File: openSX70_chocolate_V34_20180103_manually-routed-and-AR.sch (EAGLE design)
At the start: 37 parts, among them Q1 5.8A/30V/35mΩ, Q2 5.8A/30V/35mΩ, U1 ATMEGA328P_TQFP, U3 BH1750FVI-TR, Y1 CSTCE16M0V53-R0

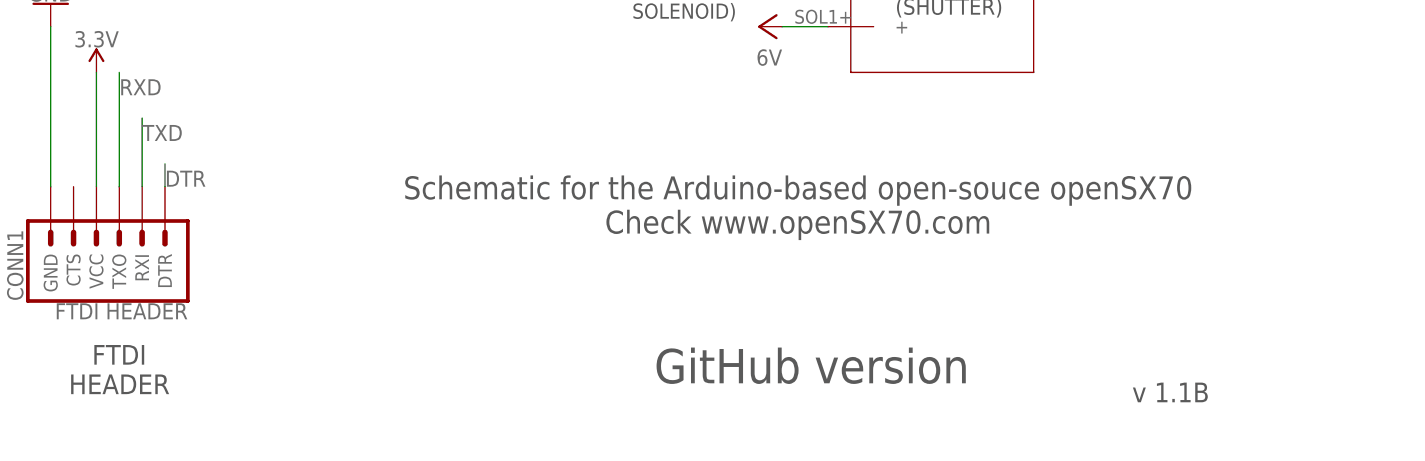
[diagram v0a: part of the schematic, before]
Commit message: Create new 3.4 "chocolate" version. Looks ok, will do more tests and send it for fabrication. Also created gerbers, remember minimun .8mm, better .6mm or .4mm.
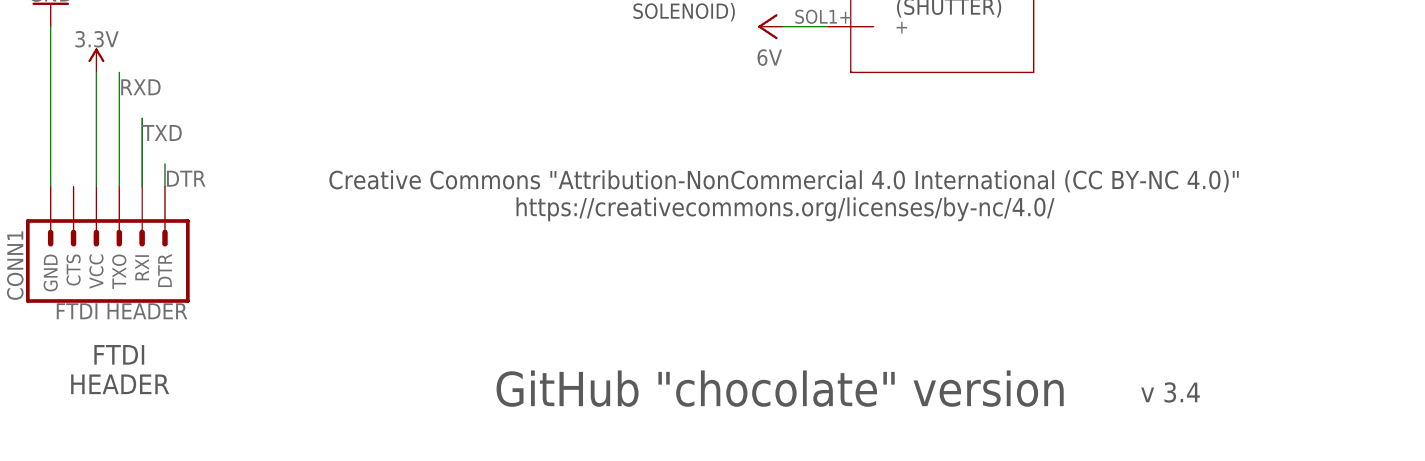
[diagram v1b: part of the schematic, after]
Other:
- note added: "Creative Commons "Attribution-NonCommercial 4.0 International (CC BY-NC 4.0)" https://creativecommons.org/licenses/by-nc/4.0/"
- note added: "GitHub "chocolate" version"
- note added: "v 3.4"
- note removed: "GitHub version"
- note removed: "Schematic for the Arduino-based open-souce openSX70 Check www.openSX70.com"
- note removed: "v 1.1B"
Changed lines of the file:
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@@
 or
 FLASH</text>
-<text x="246.38" y="2.54" size="2.1844" layer="97" align="center">v 1.1B</text>
-<text x="204.978" y="23.368" size="2.54" layer="97" align="center">Schematic for the Arduino-based open-souce openSX70
-Check www.openSX70.com</text>
-<text x="188.976" y="3.556" size="3.81" layer="97">GitHub version </text>
+<text x="246.38" y="2.54" size="2.1844" layer="97" align="center">v 3.4</text>
+<text x="203.454" y="24.638" size="2.0066" layer="97" align="center">Creative Commons "Attribution-NonCommercial 4.0 International (CC BY-NC 4.0)"
+https://creativecommons.org/licenses/by-nc/4.0/</text>
+<text x="171.196" y="1.016" size="3.81" layer="97">GitHub "chocolate" version</text>
 <polygon width="0.1524" layer="96" spacing="0.254">
 <vertex x="5.08" y="154.94"/>
